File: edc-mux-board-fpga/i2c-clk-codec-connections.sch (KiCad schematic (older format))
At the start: 72 parts, among them U52 CDCLVC1108, U53 TCA9548A, U54 TCA9555RTWR, U55 CDCLVC1108, U56 TCA9548A

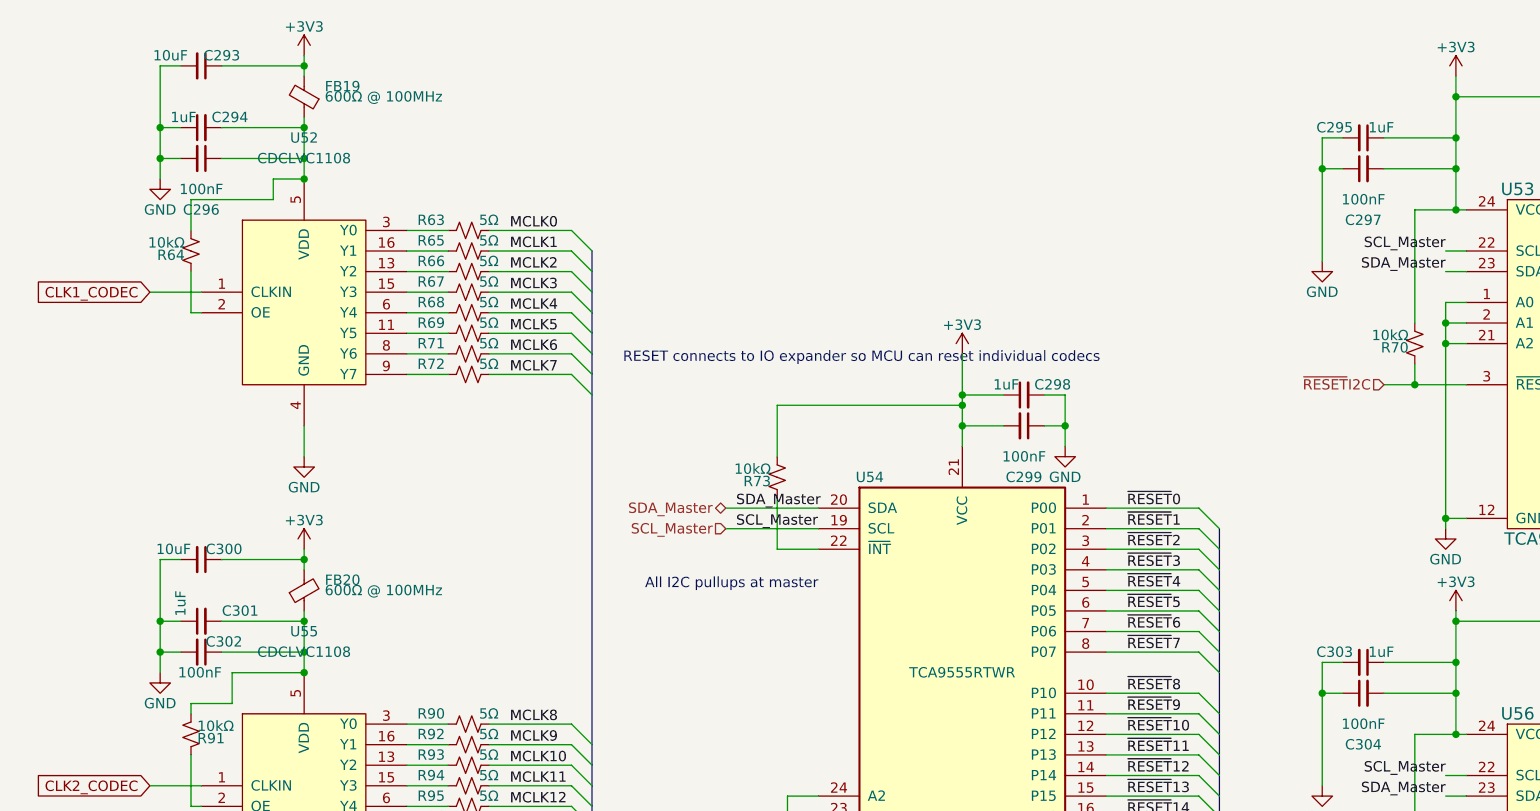
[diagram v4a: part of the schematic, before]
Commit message: assigned more footprints
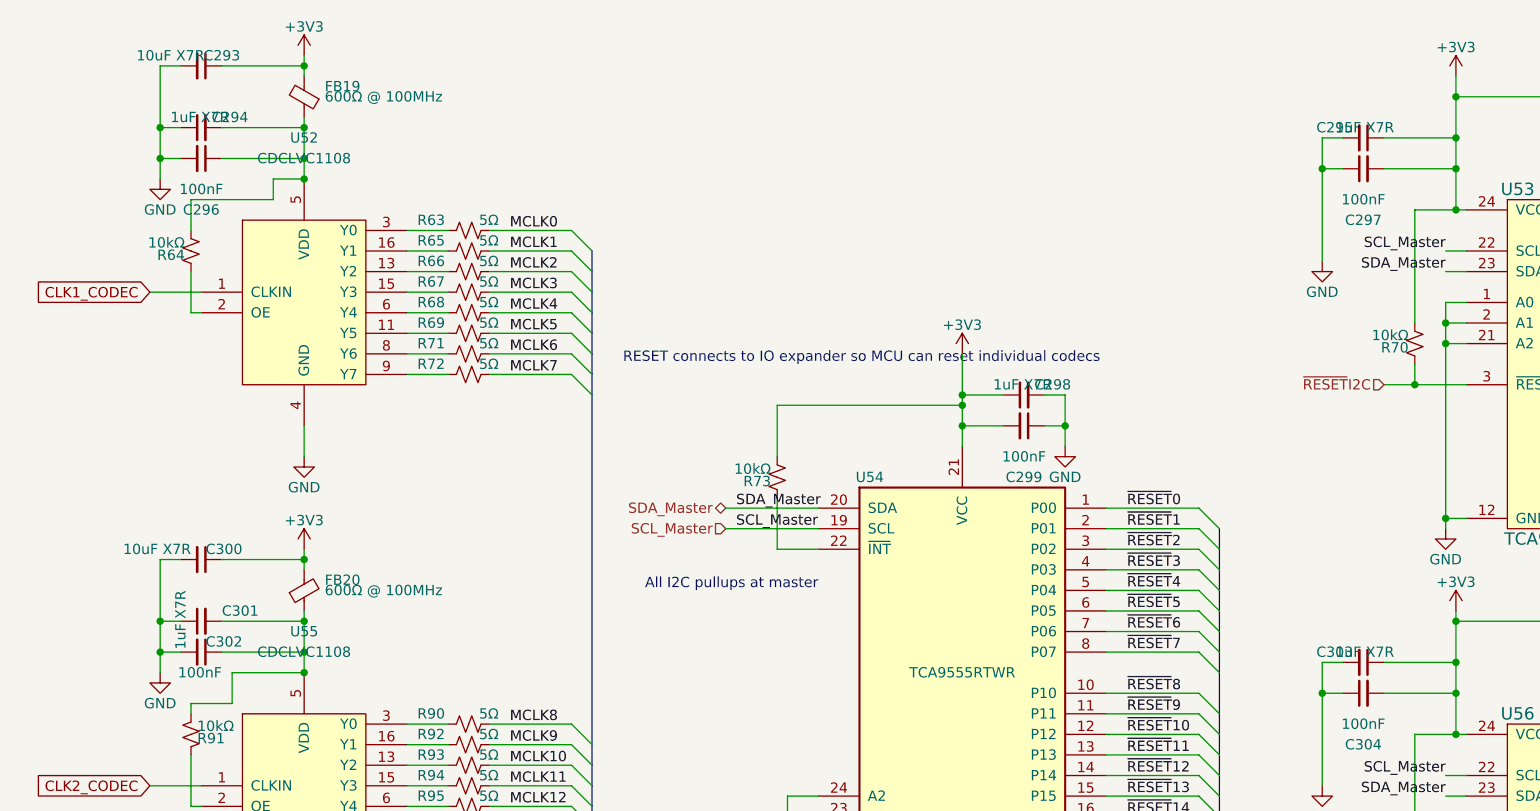
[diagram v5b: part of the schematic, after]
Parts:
- C293, C300: value 10uF -> 10uF X7R
- C294, C295, C298, C301, C303: value 1uF -> 1uF X7R
- R47, R48, R49, R50, R51, R52, R53, R54, R55, R56, R57, R58, R59, R60, R61, R62, R63, R64, R65, R66, R67, R68, R69, R70, R71, R72, R73, R74, R75, R76, R77, R78, R79, R80, R81, R82, R83, R84, R85, R86, R87, R88, R89, R90, R91, R92, R93, R94, R95, R96, R97, R98, R99: footprint (none) -> Resistor_SMD:R_0402_1005Metric

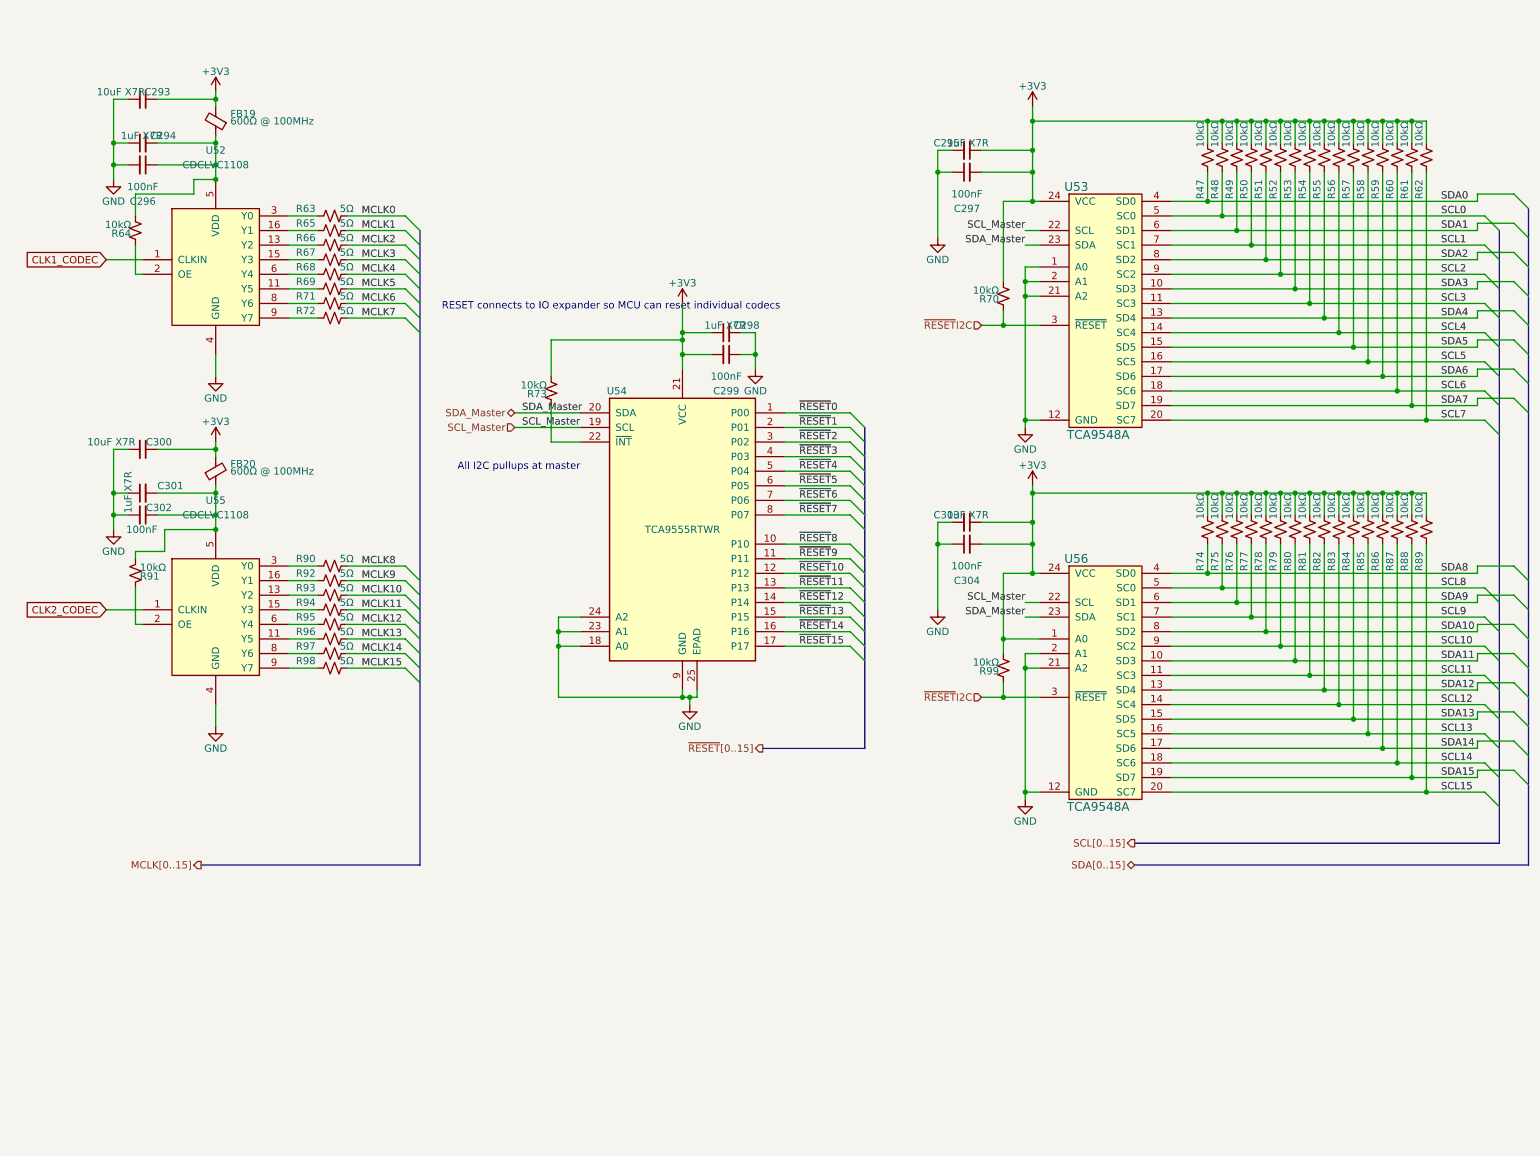
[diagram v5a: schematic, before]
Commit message: re-annotating after adding power ICs and decoupling capacitors.
Also verified most footprints, and updated schematic field data.
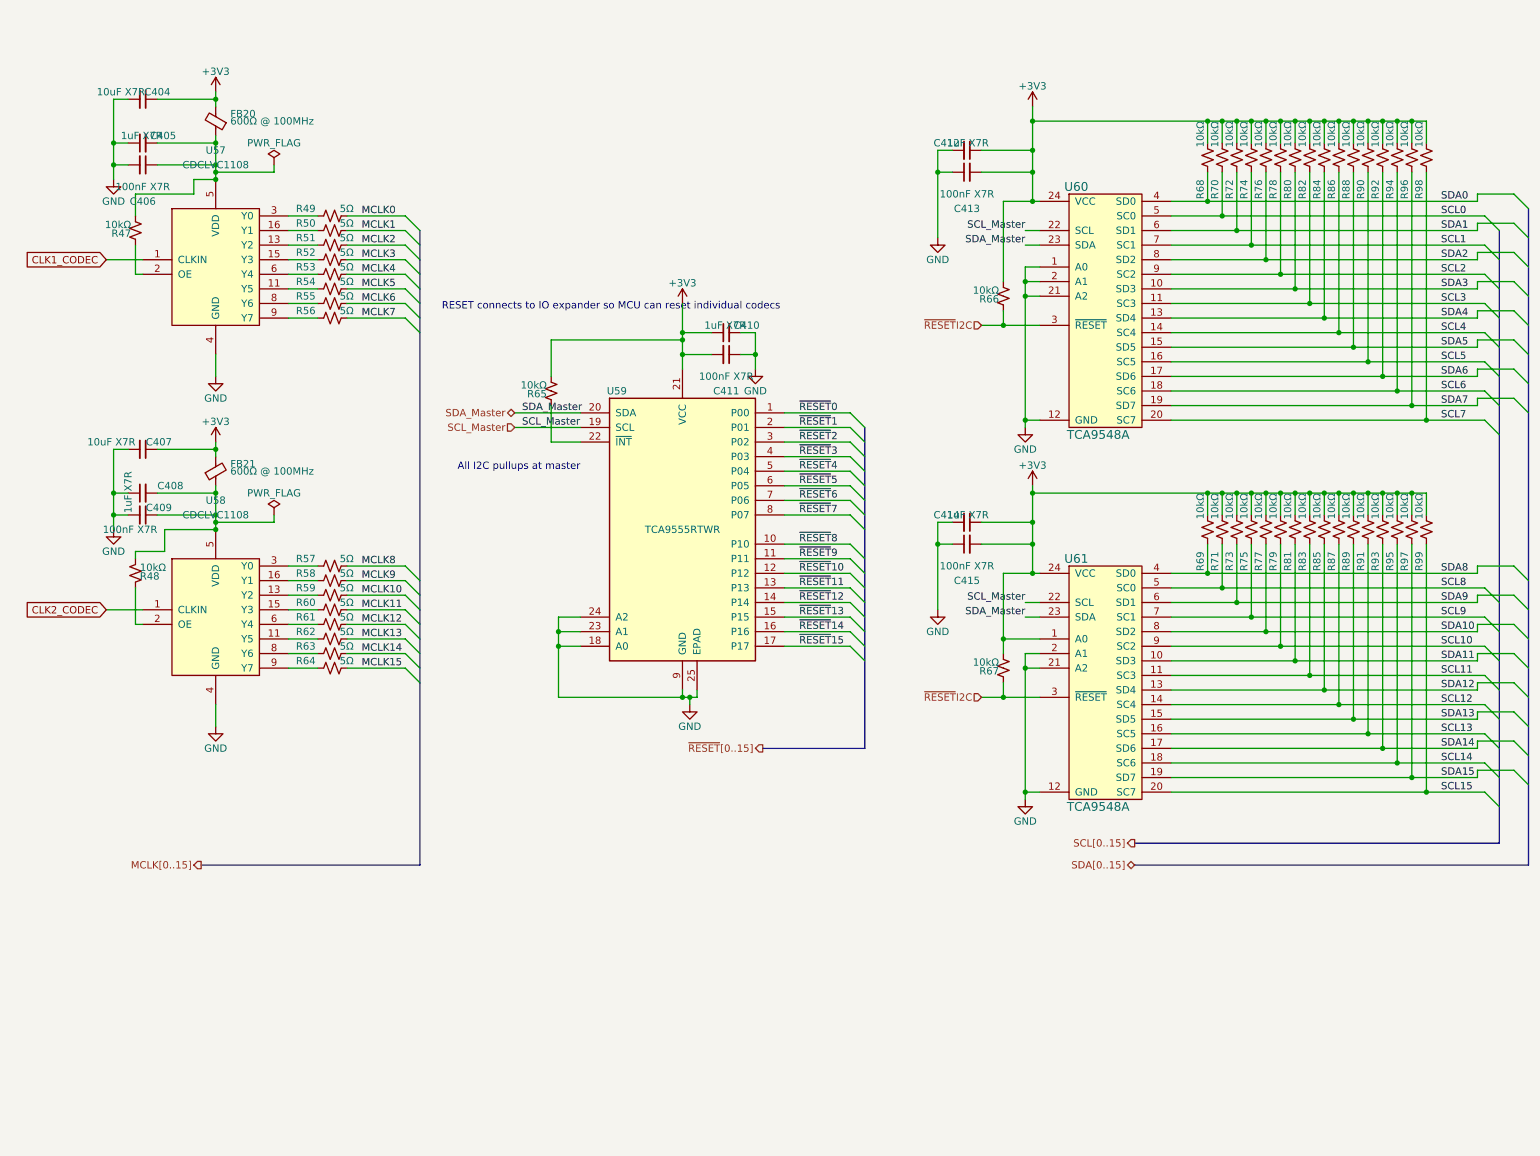
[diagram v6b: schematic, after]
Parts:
- C406: renamed from C296; value 100nF -> 100nF X7R
- C409: renamed from C302; value 100nF -> 100nF X7R
- C411: renamed from C299; value 100nF -> 100nF X7R
- C413: renamed from C297; value 100nF -> 100nF X7R
- C415: renamed from C304; value 100nF -> 100nF X7R
- R47: renamed from R64; Package ID (none) -> 0402in/1005mm
- R48: renamed from R91; Package ID (none) -> 0402in/1005mm
- R49: renamed from R63; Package ID (none) -> 0402in/1005mm
- R50: renamed from R65; Package ID (none) -> 0402in/1005mm
- R51: renamed from R66; Package ID (none) -> 0402in/1005mm
- R52: renamed from R67; Package ID (none) -> 0402in/1005mm
- R53: renamed from R68; Package ID (none) -> 0402in/1005mm
- R54: renamed from R69; Package ID (none) -> 0402in/1005mm
- R55: renamed from R71; Package ID (none) -> 0402in/1005mm
- R56: renamed from R72; Package ID (none) -> 0402in/1005mm
- R57: renamed from R90; Package ID (none) -> 0402in/1005mm
- R58: renamed from R92; Package ID (none) -> 0402in/1005mm
- R59: renamed from R93; Package ID (none) -> 0402in/1005mm
- R60: renamed from R94; Package ID (none) -> 0402in/1005mm
- R61: renamed from R95; Package ID (none) -> 0402in/1005mm
- R62: renamed from R96; Package ID (none) -> 0402in/1005mm
- R63: renamed from R97; Package ID (none) -> 0402in/1005mm
- R64: renamed from R98; Package ID (none) -> 0402in/1005mm
- R65: renamed from R73; Package ID (none) -> 0402in/1005mm
- R66: renamed from R70; Package ID (none) -> 0402in/1005mm
- R67: renamed from R99; Package ID (none) -> 0402in/1005mm
- R68: renamed from R47; Package ID (none) -> 0402in/1005mm
- R69: renamed from R74; Package ID (none) -> 0402in/1005mm
- R70: renamed from R48; Package ID (none) -> 0402in/1005mm
- R71: renamed from R75; Package ID (none) -> 0402in/1005mm
- R72: renamed from R49; Package ID (none) -> 0402in/1005mm
- R73: renamed from R76; Package ID (none) -> 0402in/1005mm
- R74: renamed from R50; Package ID (none) -> 0402in/1005mm
- R75: renamed from R77; Package ID (none) -> 0402in/1005mm
- R76: renamed from R51; Package ID (none) -> 0402in/1005mm
- R77: renamed from R78; Package ID (none) -> 0402in/1005mm
- R78: renamed from R52; Package ID (none) -> 0402in/1005mm
- R79: Package ID (none) -> 0402in/1005mm
- R80: renamed from R53; Package ID (none) -> 0402in/1005mm
- R81: renamed from R80; Package ID (none) -> 0402in/1005mm
- R82: renamed from R54; Package ID (none) -> 0402in/1005mm
- R83: renamed from R81; Package ID (none) -> 0402in/1005mm
- R84: renamed from R55; Package ID (none) -> 0402in/1005mm
- R85: renamed from R82; Package ID (none) -> 0402in/1005mm
- R86: renamed from R56; Package ID (none) -> 0402in/1005mm
- R87: renamed from R83; Package ID (none) -> 0402in/1005mm
- R88: renamed from R57; Package ID (none) -> 0402in/1005mm
- R89: renamed from R84; Package ID (none) -> 0402in/1005mm
- R90: renamed from R58; Package ID (none) -> 0402in/1005mm
- R91: renamed from R85; Package ID (none) -> 0402in/1005mm
- R92: renamed from R59; Package ID (none) -> 0402in/1005mm
- R93: renamed from R86; Package ID (none) -> 0402in/1005mm
- R94: renamed from R60; Package ID (none) -> 0402in/1005mm
- R95: renamed from R87; Package ID (none) -> 0402in/1005mm
- R96: renamed from R61; Package ID (none) -> 0402in/1005mm
- R97: renamed from R88; Package ID (none) -> 0402in/1005mm
- R98: renamed from R62; Package ID (none) -> 0402in/1005mm
- R99: renamed from R89; Package ID (none) -> 0402in/1005mm
- U57: renamed from U52; Description (none) -> 1:8 Clock Buffer; Manufacturer (none) -> Texas Instruments; Manufacturers Part Number (none) -> CDCLVC1108
- U58: renamed from U55; Description (none) -> 1:8 Clock Buffer; Manufacturer (none) -> Texas Instruments; Manufacturers Part Number (none) -> CDCLVC1108
- renumbered C293 to C404, C294 to C405, C300 to C407, C301 to C408, C298 to C410, C295 to C412, C303 to C414, FB19 to FB20, FB20 to FB21, U54 to U59, U53 to U60, U56 to U61

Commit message: Reannotating and adding more fields to components
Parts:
- C404, C407: Characteristics (none) -> CAP CER 10UF 25V X7R 1206; Description (none) -> MLCC Capacitor
- C405, C408, C410, C412, C414: Characteristics (none) -> CAP CER 1UF 25V X7R 0603; Description (none) -> MLCC Capacitor
- C406, C409, C411, C413, C415: Characteristics (none) -> CAP CER 0.1UF 25V X7R 0603; Description (none) -> MLCC Capacitor; Manufacturer (none) -> Kemet; Manufacturers Part Number (none) -> C0603C104J3RACAUTO
- FB20, FB21: footprint Capacitor_SMD:C_0805_2012Metric -> Inductor_SMD:L_0805_2012Metric; Characteristics (none) -> 600 Ohms @ 100MHz 1 Signal Line Ferrite Bead 0805 (2012 Met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; Description (none) -> Ferrite Bead; Manufacturers Part Number BLM21AG601BH1 -> BLM21AG601SZ1D
- R47, R48, R49, R50, R51, R52, R53, R54, R55, R56, R57, R58, R59, R60, R61, R62, R63, R64, R65, R66, R67, R68, R69, R70, R71, R72, R73, R74, R75, R76, R77, R78, R79, R80, R81, R82, R83, R84, R85, R86, R87, R88, R89, R90, R91, R92, R93, R94, R95, R96, R97, R98, R99: Description (none) -> Resistor
- U57, U58: Package ID (none) -> TSSOP16
- U59: Description (none) -> 16 bit IO expander; Manufacturer (none) -> Texas Instruments; Manufacturers Part Number (none) -> TCA9555; Package ID (none) -> QFN24-EP
- U60, U61: Manufacturers Part Number (none) -> TCA9548

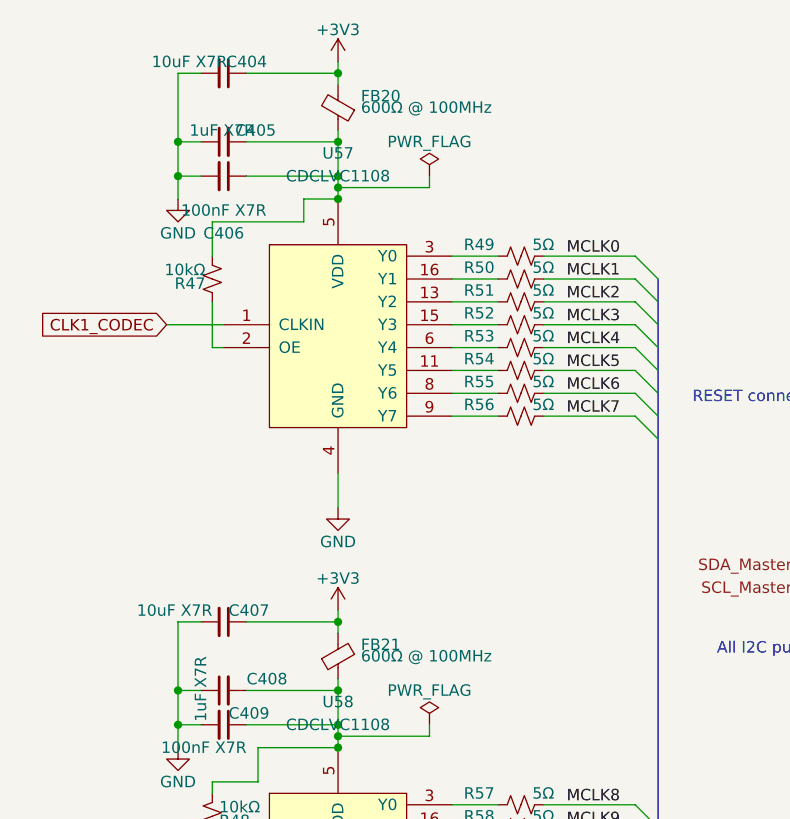
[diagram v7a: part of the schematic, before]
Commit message: Reannotating board
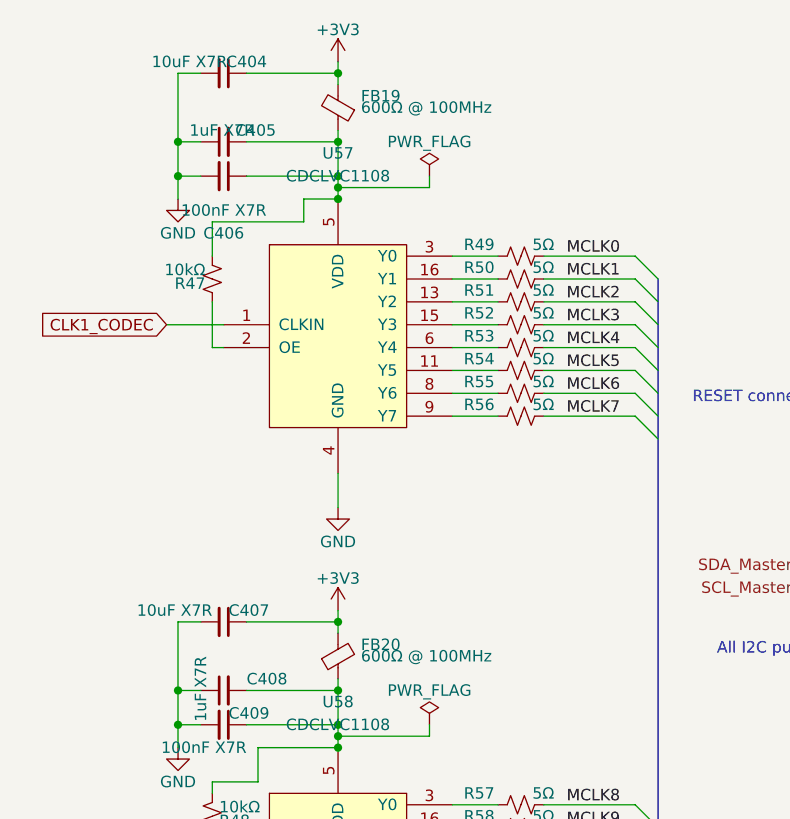
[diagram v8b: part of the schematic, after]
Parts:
- renumbered FB20 to FB19, FB21 to FB20
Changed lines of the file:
@@
 AR Path="/5CC6CC1A/5CC6D47B/647D98E2" Ref="FB?"  Part="1"
 AR Path="/5CC3E5DC/647D98E2" Ref="FB?"  Part="1"
-AR Path="/5CC6CC1A/5CCDCE34/647D98E2" Ref="FB20"  Part="1"
-F 0 "FB20" H 1850 1000 50  0000 R CNN
+AR Path="/5CC6CC1A/5CCDCE34/647D98E2" Ref="FB19"  Part="1"
+F 0 "FB19" H 1850 1000 50  0000 R CNN
 F 1 "600Ω @ 100MHz" H 1850 1050 50  0000 R CNN
 F 2 "Inductor_SMD:L_0805_2012Metric" V 1880 1050 50  0001 C CNN
@@
 AR Path="/5CC6CC1A/5CC6D47B/647D9902" Ref="FB?"  Part="1"
 AR Path="/5CC3E5DC/647D9902" Ref="FB?"  Part="1"
-AR Path="/5CC6CC1A/5CCDCE34/647D9902" Ref="FB21"  Part="1"
-F 0 "FB21" H 2050 3400 50  0000 L CNN
+AR Path="/5CC6CC1A/5CCDCE34/647D9902" Ref="FB20"  Part="1"
+F 0 "FB20" H 2050 3400 50  0000 L CNN
 F 1 "600Ω @ 100MHz" H 2050 3450 50  0000 L CNN
 F 2 "Inductor_SMD:L_0805_2012Metric" V 1880 3450 50  0001 C CNN
@@
 	8250 6150 10950 6150
 $Comp
-L power:PWR_FLAG #FLG06
+L power:PWR_FLAG #FLG05
 U 1 1 5D29107A
 P 2350 1350
-F 0 "#FLG06" H 2350 1425 50  0001 C CNN
+F 0 "#FLG05" H 2350 1425 50  0001 C CNN
 F 1 "PWR_FLAG" H 2350 1500 50  0000 C CNN
 F 2 "" H 2350 1350 50  0001 C CNN
@@
 	1950 1400 1950 1450
 $Comp
-L power:PWR_FLAG #FLG07
+L power:PWR_FLAG #FLG06
 U 1 1 5D2B45F0
 P 2350 3750
-F 0 "#FLG07" H 2350 3825 50  0001 C CNN
+F 0 "#FLG06" H 2350 3825 50  0001 C CNN
 F 1 "PWR_FLAG" H 2350 3900 50  0000 C CNN
 F 2 "" H 2350 3750 50  0001 C CNN
